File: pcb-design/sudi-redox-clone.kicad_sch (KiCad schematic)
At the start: 113 parts, among them J1 RJ12_LEFT, J2 0.91 OLED, J3 RJ12_RIGHT, J5 USB_C, J7 ARMJTAG, J8 BatCon, K1 KEYSW, K10 KEYSW, K11 KEYSW, K12 KEYSW, K13 KEYSW, K14 KEYSW, K15 KEYSW, K16 KEYSW, K17 KEYSW, K18 KEYSW, K2 KEYSW, K3 KEYSW, K4 KEYSW, K5 KEYSW, K6 KEYSW, K7 KEYSW, K8 KEYSW, K9 KEYSW, SW1 RST, U4 AMS1117-3.3, U5 nRF51x22-QFxx, U6 TP4056, U8 MCP23017_SS, Y2 16MHz

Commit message: [minggu 7 juli 12:12] create pcb cut profile
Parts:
- removed C8: 100nF, symbol Device:C
- removed J5: USB_C, symbol Connector:USB_C_Receptacle_USB2.0_14P
- removed SW1: RST, symbol Switch:SW_Push
- added J4: USBC_PWR_ONLY, Connector_USB:USB_C_Receptacle_GCT_USB4125-xx-x-0190_6P_TopMnt_Horizontal, symbol Connector:USB_C_Receptacle_PowerOnly_6P
- C1, C11, C12, C13, C14, C15, C16, C17, C18, C19, C2, C20, C21, C3, C4: footprint (none) -> Capacitor_SMD:C_0805_2012Metric_Pad1.18x1.45mm_HandSolder
- FB1, L1, L2, L3: footprint (none) -> Inductor_SMD:L_0603_1608Metric_Pad1.05x0.95mm_HandSolder
- J1, J3: footprint Connector_RJ:RJ12_Amphenol_54601 -> Connector_RJ:RJ25_Wayconn_MJEA-660X1_Horizontal
- J2: footprint KiCad-SSD1306-0.91-OLED-4pin-128x32:SSD1306-0.91-OLED-4pin-128x32 -> Connector_PinHeader_2.54mm:PinHeader_1x04_P2.54mm_Vertical
- J7: footprint (none) -> Connector_PinHeader_2.54mm:PinHeader_2x05_P2.54mm_Horizontal
- K2, K3: footprint canadian_footprints:Mx_Alps_150-dualsided -> canadian_footprints:Mx_Alps_100-dualside
- Y2: footprint (none) -> Crystal:Crystal_HC50_Vertical
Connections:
- net +3V7: now also J1.5, J3.5; no longer J1.6, J3.6
- net +5V: now also J1.6, J3.6
- net GND: now also J1.1, J3.1, J4.A12 (GND), J4.B12 (GND), J4.S1 (SHIELD); no longer J1.2, J3.2
- net SCL: now also J1.3, J3.3; no longer J1.4, J3.4
- net SDA: now also J1.4, J3.4; no longer J1.5, J3.5
- net Tx: now also J1.2, J3.2; no longer J1.3, J3.3
- net at R3.1: now also J4.A5 (CC1)
- net at R4.1: now also J4.B5 (CC2)
- net at FB1.1: now also J4.A9 (VBUS), J4.B9 (VBUS)
- no-connect marks 25 -> 23
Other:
- moved on the sheet: C2, C3, J1, R3, R4

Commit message: [minggu 7 juli 19:32] finish PCB Layout
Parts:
- removed H1, H2: MountingHole_Pad, MountingHole:MountingHole_3.2mm_M3_DIN965_Pad, symbol Mechanical:MountingHole_Pad
- D10, D11, D12, D16, D17, D18, D22, D23, D24, D28, D43, D44, D45, D46, D47, D48, D5, D6: footprint LED_SMD:LED_WS2812B_PLCC4_5.0x5.0mm_P3.2mm -> CustomWS2185BFootPrint:LED_WS2812B_PLCC4_5.0x5.0mm_P3.2mm
- K1, K10, K11, K12, K13, K14, K15, K16, K17, K18, K2, K3, K4, K5, K6, K7, K8, K9: footprint canadian_footprints:Mx_Alps_100-dualside -> keyswitches.pretty-master:Kailh_socket_MX_optional_reversible_platemount
- R1, R2, R3, R4, R5, R6, R7: footprint Resistor_SMD:R_1206_3216Metric -> Resistor_SMD:R_0805_2012Metric_Pad1.20x1.40mm_HandSolder
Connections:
- net GND: no longer H8.1, H9.1

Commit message: add some route progress
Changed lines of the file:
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@@
 		(at 172.72 109.22)
 		(size 29.21 16.51)
-		(fields_autoplaced yes)
 		(stroke
 			(width 0.1524)
@@
 		)
 		(property "Sheetname" "Receiver"
-			(at 172.72 107.8734 0)
+			(at 178.562 118.618 0)
 			(effects
 				(font

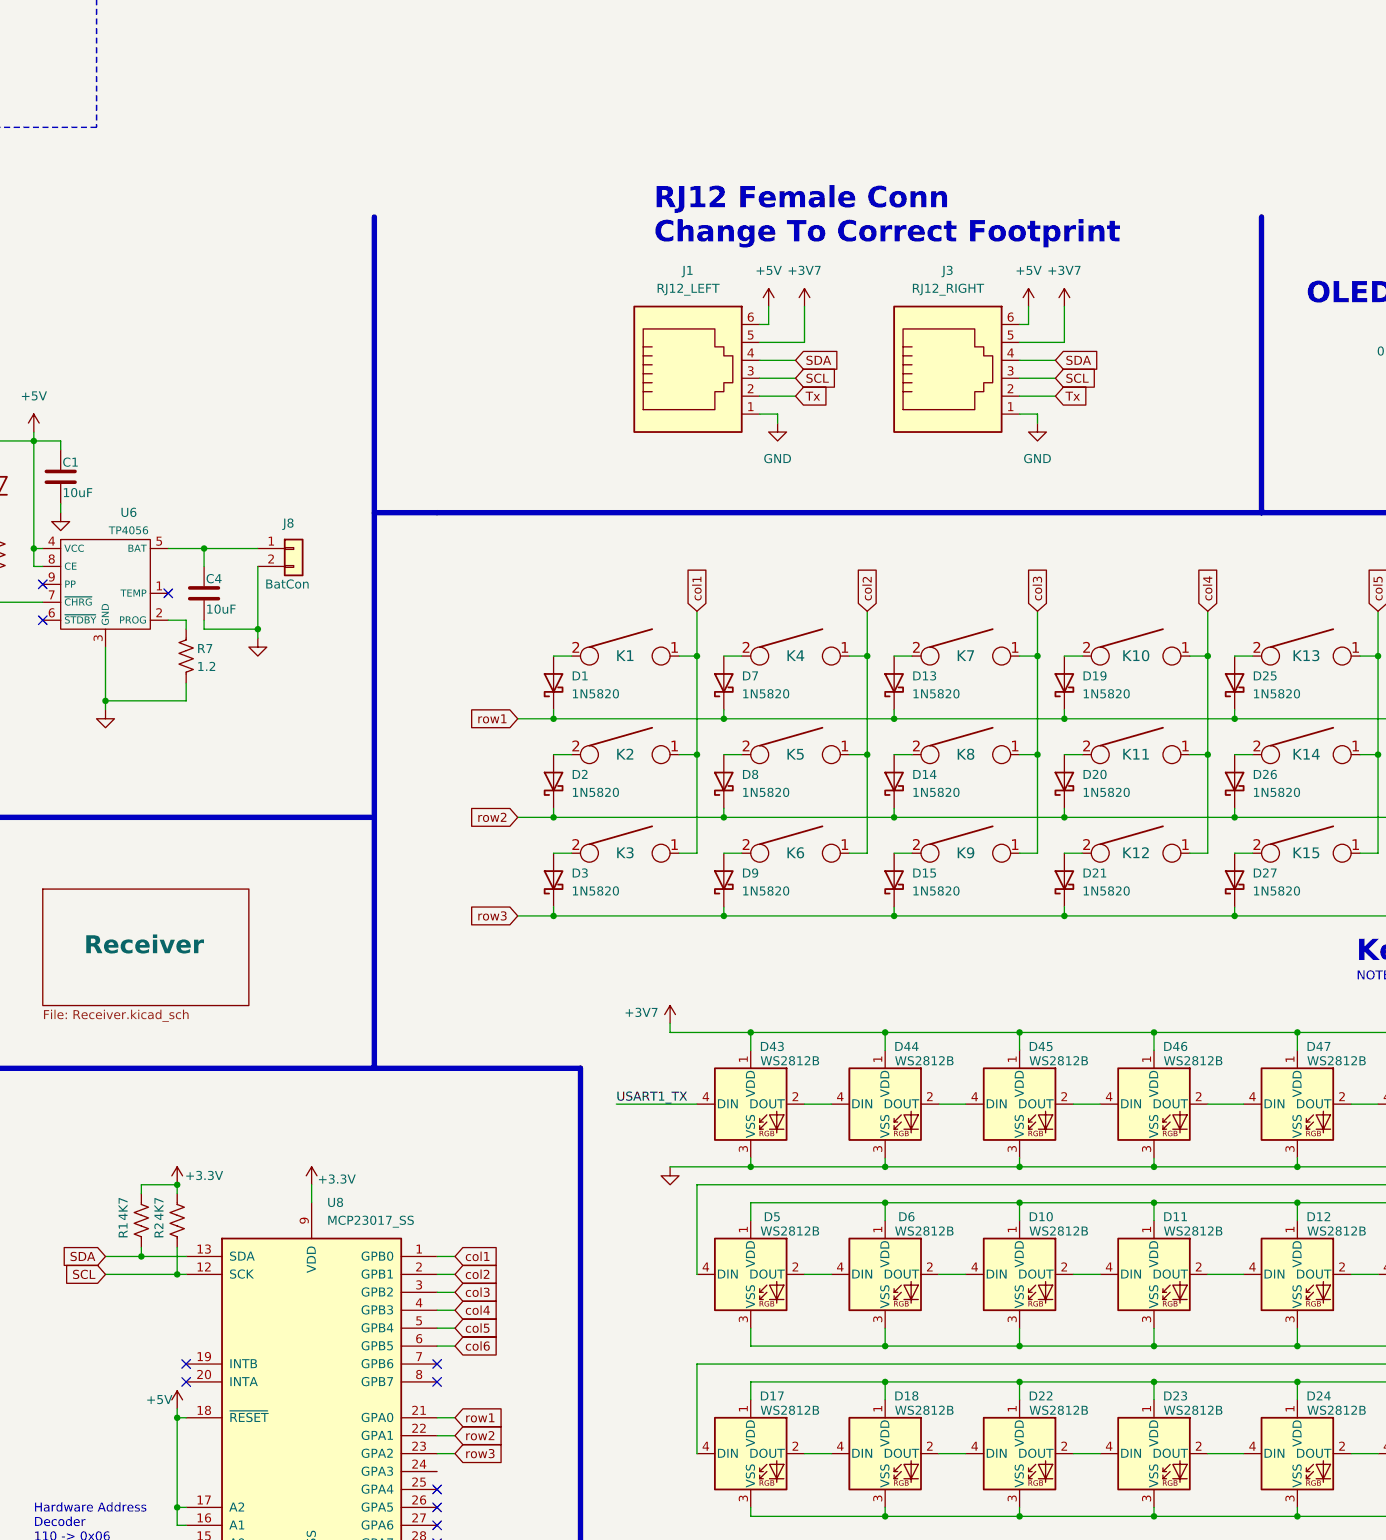
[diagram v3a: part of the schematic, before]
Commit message: [rabu 24 juli 20:17] finish keyboard layout - todo receiver
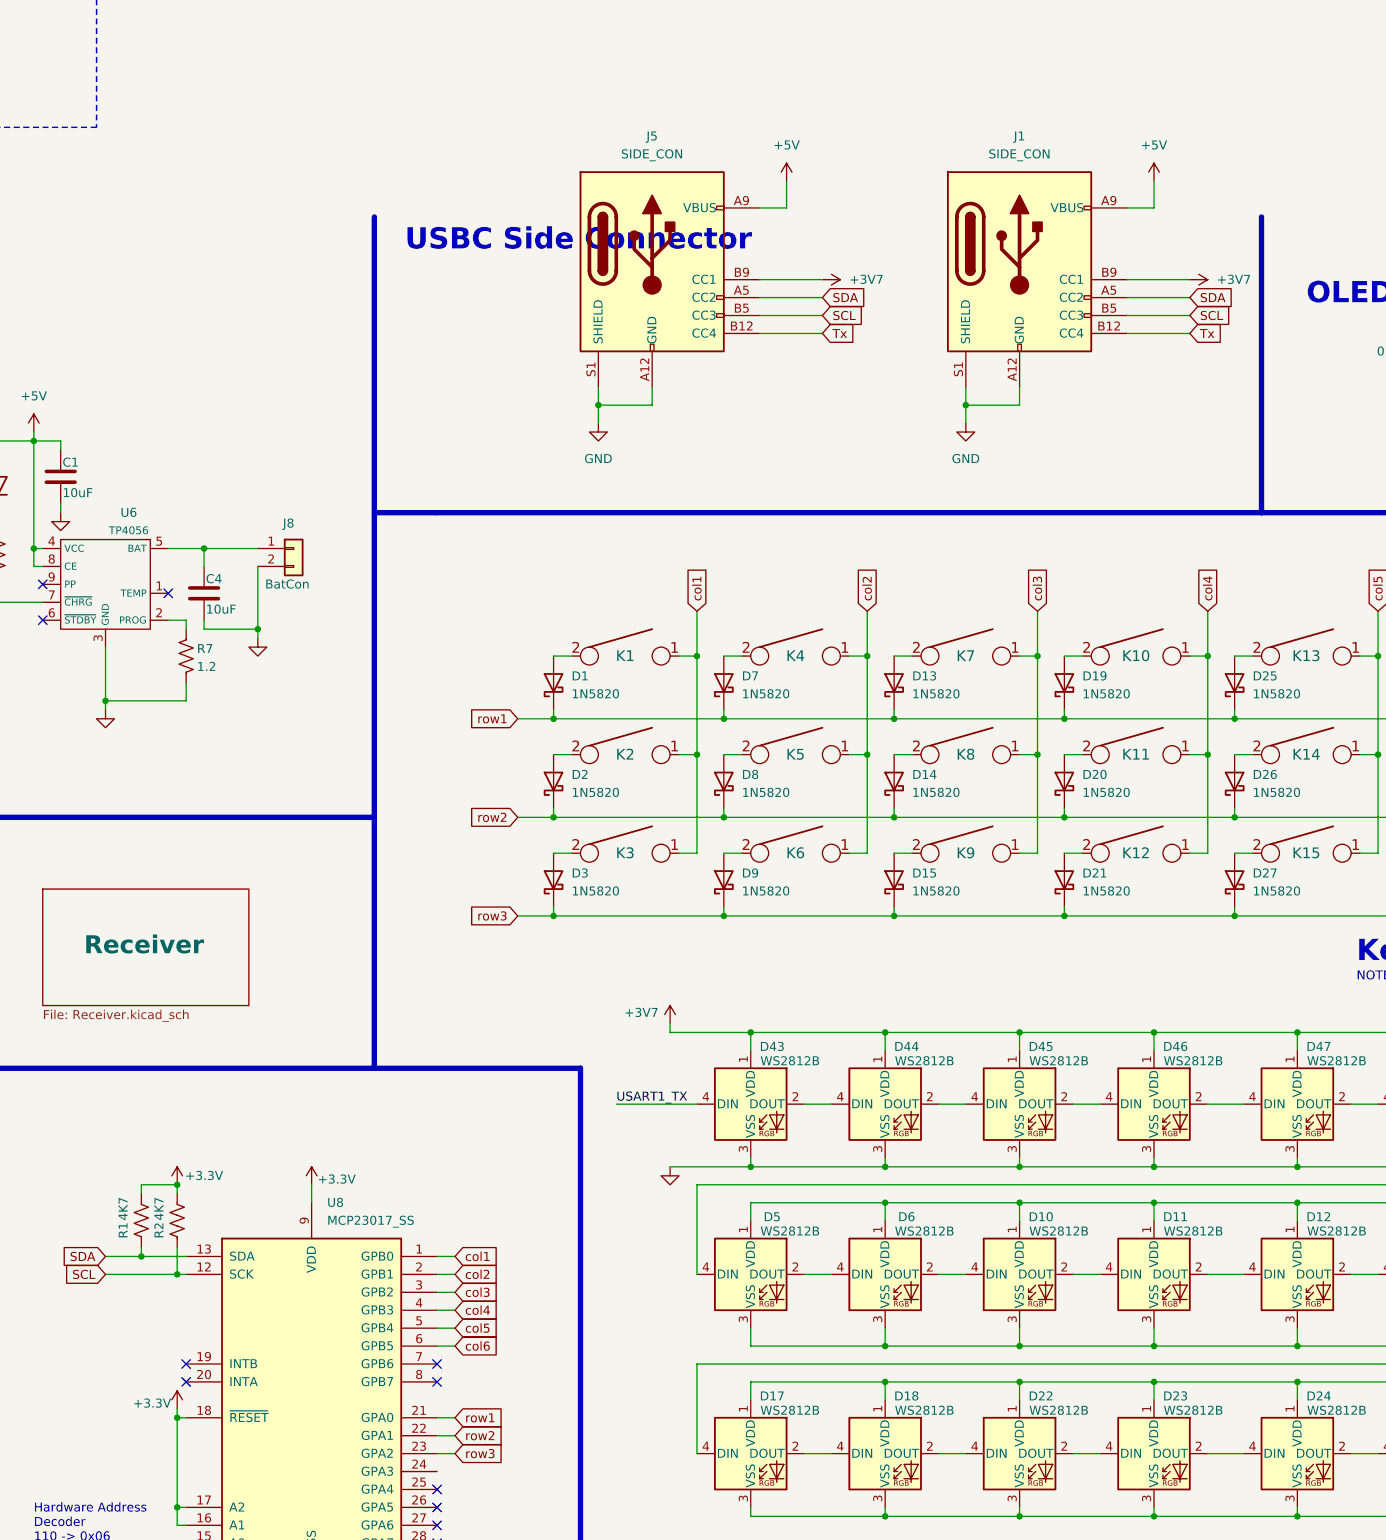
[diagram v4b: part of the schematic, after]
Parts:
- removed J1: RJ12_LEFT, Connector_RJ:RJ25_Wayconn_MJEA-660X1_Horizontal, symbol Connector:RJ12
- removed J3: RJ12_RIGHT, Connector_RJ:RJ25_Wayconn_MJEA-660X1_Horizontal, symbol Connector:RJ12
- added J1, J5: SIDE_CON, Connector_USB:USB_C_Receptacle_GCT_USB4125-xx-x-0190_6P_TopMnt_Horizontal, symbol Connector:USB_C_Receptacle_PowerOnly_6P
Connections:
- net +3.3V: now also U8.16 (A1), U8.17 (A2), U8.18 (~{RESET})
- net +3V7: now also J1.B9 (CC1), J5.B9 (CC1)
- net +5V: now also J1.A9 (VBUS), J5.A9 (VBUS); no longer U8.16 (A1), U8.17 (A2), U8.18 (~{RESET})
- net GND: now also J1.A12 (GND), J1.S1 (SHIELD), J5.A12 (GND), J5.S1 (SHIELD)
- net SCL: now also J1.B5 (CC3), J5.B5 (CC3)
- net SDA: now also J1.A5 (CC2), J5.A5 (CC2)
- net Tx: now also J1.B12 (CC4), J5.B12 (CC4)
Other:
- note added: "USBC Side Connector"
- note removed: "RJ12 Female Conn Change To Correct Footprint"
